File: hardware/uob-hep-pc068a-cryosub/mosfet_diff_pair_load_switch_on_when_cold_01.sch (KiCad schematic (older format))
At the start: 22 parts, among them Q1 BSS127S, Q2 BSS127S, Q3 FDD306P

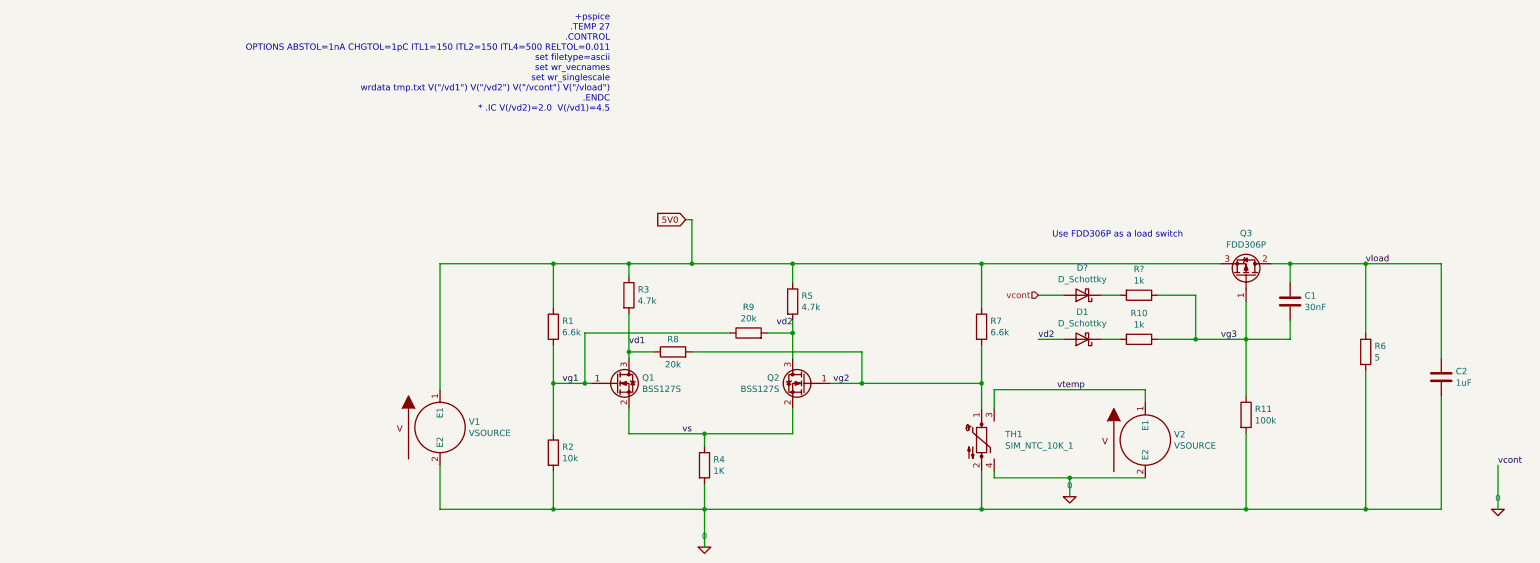
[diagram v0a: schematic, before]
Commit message: Tuning simulation to change on/off temperature. Then making the resulting changes to BoM
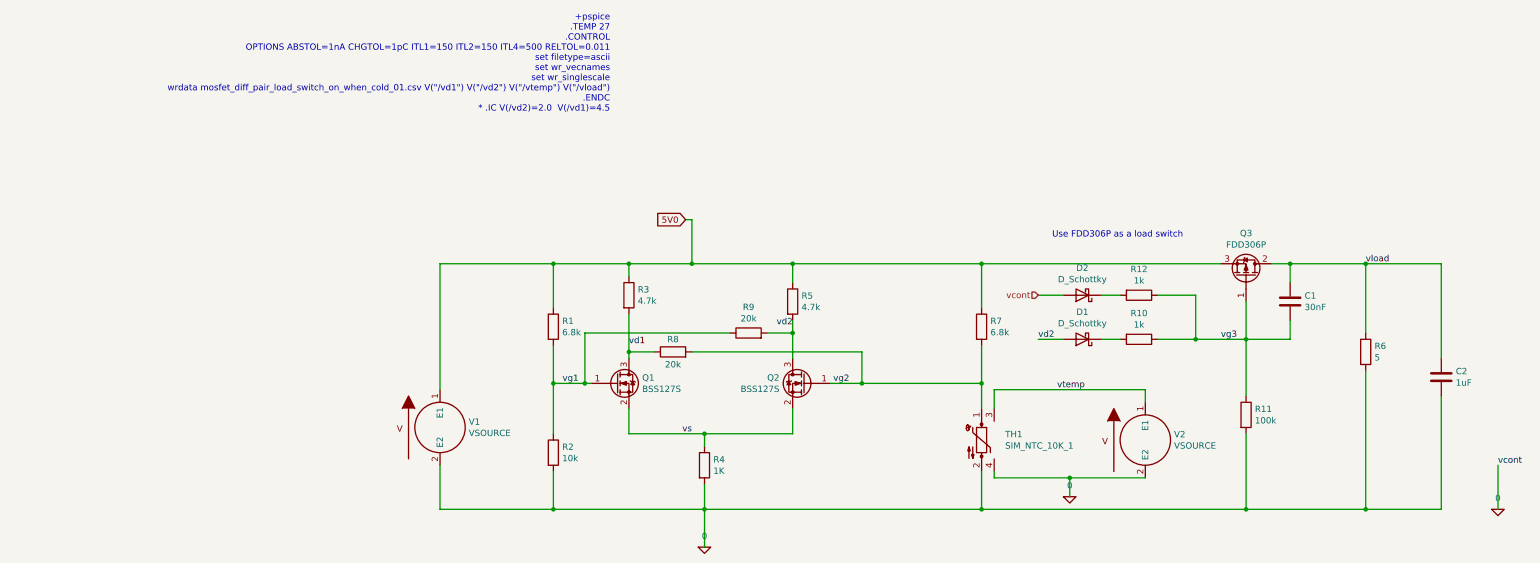
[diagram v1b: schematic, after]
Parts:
- R1, R7: value 6.6k -> 6.8k
- gave numbers to parts that had none: 2
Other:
- note added: "+pspice \n.TEMP 27\n.CONTROL \nOPTIONS ABSTOL=1nA CHGTOL=1pC ITL1=150 ITL2=150 ITL4=500 RELTOL=0.011\nset filetype=ascii\nset wr_vecnames\nset wr_singlescale\nwrdata mosfet_diff_pair_load_switch_on_when_cold_01.csv V("/vd1") V("/vd2") V("/vtemp") V("/vload")\n.ENDC\n* .IC V(/vd2)=2.0 V(/vd1)=4.5"
- note removed: "+pspice \n.TEMP 27\n.CONTROL \nOPTIONS ABSTOL=1nA CHGTOL=1pC ITL1=150 ITL2=150 ITL4=500 RELTOL=0.011\nset filetype=ascii\nset wr_vecnames\nset wr_singlescale\nwrdata tmp.txt V("/vd1") V("/vd2") V("/vcont") V("/vload")\n.ENDC\n* .IC V(/vd2)=2.0 V(/vd1)=4.5"
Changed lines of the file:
@@
 P 6750 3400
 F 0 "R7" H 6820 3445 50  0000 L CNN
-F 1 "6.6k" H 6820 3355 50  0000 L CNN
+F 1 "6.8k" H 6820 3355 50  0000 L CNN
 F 2 "Resistor_SMD:R_0603_1608Metric_Pad0.98x0.95mm_HandSolder" V 6680 3400 50  0001 C CNN
 F 3 "~" H 6750 3400 50  0001 C CNN
@@
 	2450 4500 2450 4850
 Text Notes 3800 1700 2    50   ~ 0
-+pspice \n.TEMP 27\n.CONTROL \nOPTIONS ABSTOL=1nA CHGTOL=1pC ITL1=150 ITL2=150 ITL4=500 RELTOL=0.011\nset filetype=ascii\nset wr_vecnames\nset wr_singlescale\nwrdata tmp.txt V("/vd1") V("/vd2") V("/vcont") V("/vload")\n.ENDC\n* .IC V(/vd2)=2.0  V(/vd1)=4.5
++pspice \n.TEMP 27\n.CONTROL \nOPTIONS ABSTOL=1nA CHGTOL=1pC ITL1=150 ITL2=150 ITL4=500 RELTOL=0.011\nset filetype=ascii\nset wr_vecnames\nset wr_singlescale\nwrdata mosfet_diff_pair_load_switch_on_when_cold_01.csv V("/vd1") V("/vd2") V("/vtemp") V("/vload")\n.ENDC\n* .IC V(/vd2)=2.0  V(/vd1)=4.5
 Wire Wire Line
 	5550 3850 5800 3850
@@
 P 3350 3400
 F 0 "R1" H 3420 3445 50  0000 L CNN
-F 1 "6.6k" H 3420 3355 50  0000 L CNN
+F 1 "6.8k" H 3420 3355 50  0000 L CNN
 F 2 "Resistor_SMD:R_0603_1608Metric_Pad0.98x0.95mm_HandSolder" V 3280 3400 50  0001 C CNN
 F 3 "~" H 3350 3400 50  0001 C CNN
@@
 	8850 4850 9800 4850
 $Comp
-L Device:R R?
+L Device:R R12
 U 1 1 607FC873
 P 8000 3150
-F 0 "R?" V 7793 3150 50  0000 C CNN
+F 0 "R12" V 7793 3150 50  0000 C CNN
 F 1 "1k" V 7884 3150 50  0000 C CNN
 F 2 "Resistor_SMD:R_0603_1608Metric_Pad0.98x0.95mm_HandSolder" V 7930 3150 50  0001 C CNN
@@
 	7850 3150 7700 3150
 $Comp
-L Device:D_Schottky D?
+L Device:D_Schottky D2
 U 1 1 607FC883
 P 7550 3150
-F 0 "D?" H 7550 2933 50  0000 C CNN
+F 0 "D2" H 7550 2933 50  0000 C CNN
 F 1 "D_Schottky" H 7550 3024 50  0000 C CNN
 F 2 "" H 7550 3150 50  0001 C CNN
@@
 vcont
 $Comp
-L pspice:0 #GND?
+L pspice:0 #GND0101
 U 1 1 6080CABD
 P 10850 4850
-F 0 "#GND?" H 10850 4750 50  0001 C CNN
+F 0 "#GND0101" H 10850 4750 50  0001 C CNN
 F 1 "0" H 10850 4939 50  0000 C CNN
 F 2 "" H 10850 4850 50  0001 C CNN

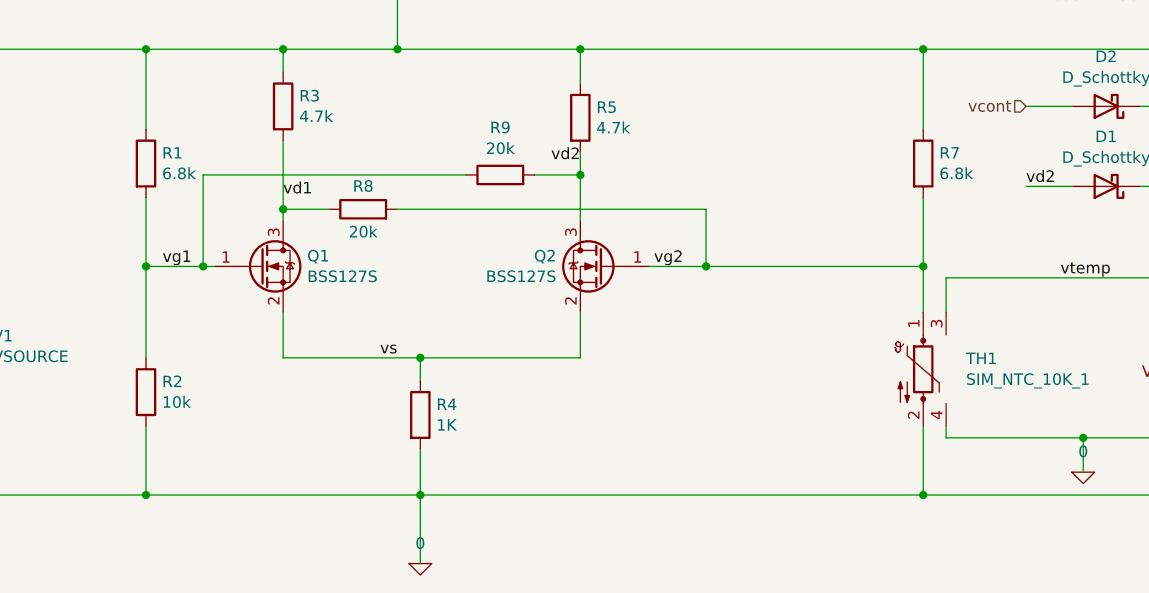
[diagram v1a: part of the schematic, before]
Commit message: Changed mosfet from bss127s --> irlml2402 (which has lower threshold voltage and higher transconductance
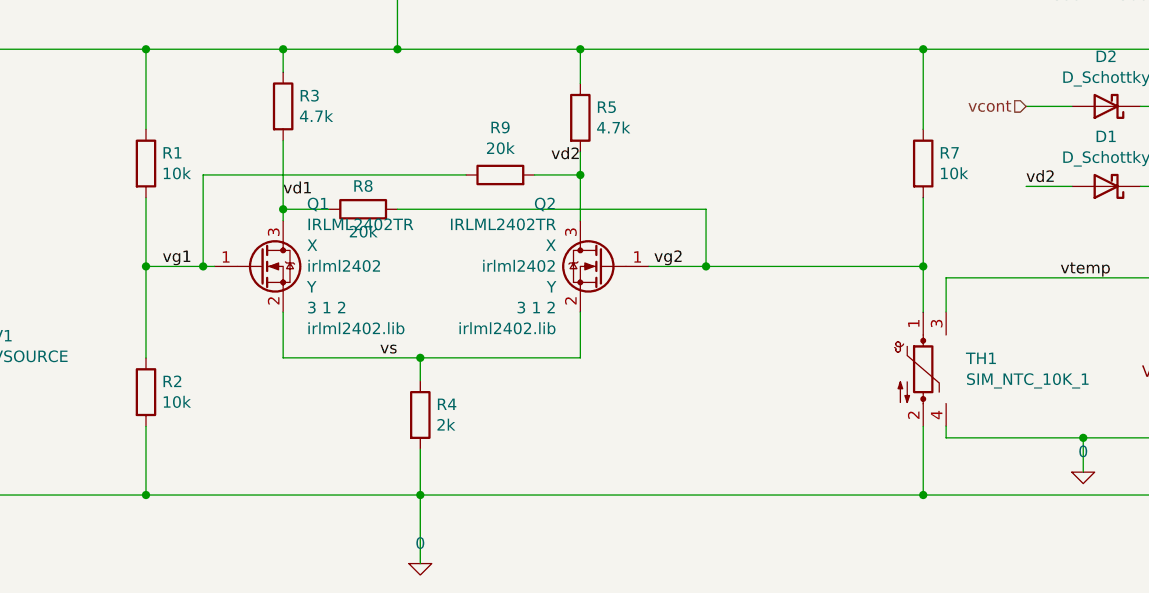
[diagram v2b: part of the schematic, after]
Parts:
- removed Q1, Q2: BSS127S, Package_TO_SOT_SMD:SOT-23, symbol Transistor_FET:BSS127S
- added Q1, Q2: IRLML2402TR, Package_TO_SOT_SMD:SOT-23, symbol kicad_cryosub_simlib:IRLML2402TR
- R1, R7: value 6.8k -> 10k
- R4: value 1K -> 2k
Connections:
- net vd1: now also Q1.3 (D)
- net vd2: now also Q2.3 (D)
- net vg1: now also Q1.1 (G)
- net vg2: now also Q2.1 (G)
- net vs: now also Q1.2 (S), Q2.2 (S)
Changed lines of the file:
@@
 P 6750 3400
 F 0 "R7" H 6820 3445 50  0000 L CNN
-F 1 "6.8k" H 6820 3355 50  0000 L CNN
+F 1 "10k" H 6820 3355 50  0000 L CNN
 F 2 "Resistor_SMD:R_0603_1608Metric_Pad0.98x0.95mm_HandSolder" V 6680 3400 50  0001 C CNN
 F 3 "~" H 6750 3400 50  0001 C CNN
@@
 Wire Wire Line
 	4450 3600 5800 3600
-$Comp
-L Transistor_FET:BSS127S Q2
-U 1 1 605C1A8E
-P 5350 3850
-F 0 "Q2" H 5555 3895 50  0000 L CNN
-F 1 "BSS127S" H 5555 3805 50  0000 L CNN
-F 2 "Package_TO_SOT_SMD:SOT-23" H 5550 3775 50  0001 L CIN
-F 3 "http://www.diodes.com/assets/Datasheets/BSS127.pdf" H 5350 3850 50  0001 L CNN
-F 4 "X" H 5350 3850 50  0001 C CNN "Spice_Primitive"
-F 5 "BSS127_L0" H 5350 3850 50  0001 C CNN "Spice_Model"
-F 6 "Y" H 5350 3850 50  0001 C CNN "Spice_Netlist_Enabled"
-F 7 "./IFX-Power_OptiMOS_N-channel_small_signal_MOSFET_240V_250V_400V_600V_Spice-web.lib" H 5350 3850 50  0001 C CNN "Spice_Lib_File"
-F 8 "3 1 2" H 5350 3850 50  0001 C CNN "Spice_Node_Sequence"
-	1    5350 3850
-	-1   0    0    -1
-$EndComp
 Connection ~ 4550 4850
 Wire Wire Line
@@
 Connection ~ 5250 3450
 $Comp
-L Transistor_FET:BSS127S Q1
-U 1 1 605BE7F9
-P 3850 3850
-F 0 "Q1" H 4055 3895 50  0000 L CNN
-F 1 "BSS127S" H 4055 3805 50  0000 L CNN
-F 2 "Package_TO_SOT_SMD:SOT-23" H 4050 3775 50  0001 L CIN
-F 3 "http://www.diodes.com/assets/Datasheets/BSS127.pdf" H 3850 3850 50  0001 L CNN
-F 4 "X" H 3850 3850 50  0001 C CNN "Spice_Primitive"
-F 5 "BSS127_L0" H 3850 3850 50  0001 C CNN "Spice_Model"
-F 6 "Y" H 3850 3850 50  0001 C CNN "Spice_Netlist_Enabled"
-F 7 "./IFX-Power_OptiMOS_N-channel_small_signal_MOSFET_240V_250V_400V_600V_Spice-web.lib" H 3850 3850 50  0001 C CNN "Spice_Lib_File"
-F 8 "3 1 2 " H 3850 3850 50  0001 C CNN "Spice_Node_Sequence"
-	1    3850 3850
-	1    0    0    -1
-$EndComp
-$Comp
 L Device:R R5
 U 1 1 605937CE
@@
 P 3350 3400
 F 0 "R1" H 3420 3445 50  0000 L CNN
-F 1 "6.8k" H 3420 3355 50  0000 L CNN
+F 1 "10k" H 3420 3355 50  0000 L CNN
 F 2 "Resistor_SMD:R_0603_1608Metric_Pad0.98x0.95mm_HandSolder" V 3280 3400 50  0001 C CNN
 F 3 "~" H 3350 3400 50  0001 C CNN
@@
 P 4550 4500
 F 0 "R4" H 4620 4545 50  0000 L CNN
-F 1 "1K" H 4620 4455 50  0000 L CNN
+F 1 "2k" H 4620 4455 50  0000 L CNN
 F 2 "Resistor_SMD:R_0603_1608Metric_Pad0.98x0.95mm_HandSolder" V 4480 4500 50  0001 C CNN
 F 3 "~" H 4550 4500 50  0001 C CNN
@@
 Text Label 10850 4500 0    50   ~ 0
 vcont
+$Comp
+L kicad_cryosub_simlib:IRLML2402TR Q1
+U 1 1 60A01665
+P 3850 3850
+F 0 "Q1" H 4054 4123 50  0000 L CNN
+F 1 "IRLML2402TR" H 4054 4032 50  0000 L CNN
+F 2 "Package_TO_SOT_SMD:SOT-23" H 4050 3775 50  0001 L CIN
+F 3 "https://docs.rs-online.com/c4e5/0900766b80afb7ed.pdf" H 3850 3850 50  0001 L CNN
+F 4 "X" H 4054 3941 50  0000 L CNN "Spice_Primitive"
+F 5 "irlml2402" H 4054 3850 50  0000 L CNN "Spice_Model"
+F 6 "Y" H 4054 3759 50  0000 L CNN "Spice_Netlist_Enabled"
+F 7 "3 1 2" H 4054 3668 50  0000 L CNN "Spice_Node_Sequence"
+F 8 "irlml2402.lib" H 4054 3577 50  0000 L CNN "Spice_Lib_File"
+	1    3850 3850
+	1    0    0    -1
+$EndComp
+$Comp
+L kicad_cryosub_simlib:IRLML2402TR Q2
+U 1 1 60A0FCD3
+P 5350 3850
+F 0 "Q2" H 5555 4123 50  0000 L CNN
+F 1 "IRLML2402TR" H 5555 4032 50  0000 L CNN
+F 2 "Package_TO_SOT_SMD:SOT-23" H 5550 3775 50  0001 L CIN
+F 3 "https://docs.rs-online.com/c4e5/0900766b80afb7ed.pdf" H 5350 3850 50  0001 L CNN
+F 4 "X" H 5555 3941 50  0000 L CNN "Spice_Primitive"
+F 5 "irlml2402" H 5555 3850 50  0000 L CNN "Spice_Model"
+F 6 "Y" H 5555 3759 50  0000 L CNN "Spice_Netlist_Enabled"
+F 7 "3 1 2" H 5555 3668 50  0000 L CNN "Spice_Node_Sequence"
+F 8 "irlml2402.lib" H 5555 3577 50  0000 L CNN "Spice_Lib_File"
+	1    5350 3850
+	-1   0    0    -1
+$EndComp
 $EndSCHEMATC
